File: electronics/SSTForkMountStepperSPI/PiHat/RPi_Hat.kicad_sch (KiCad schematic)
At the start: 32 parts, among them CON1 BARREL_JACK, J1 RJ12, J3 RA_STEP, J4 DEC_ENC, J5 RA_ENC, J6 DEC_STEP, Q1 Si2369DS, SW1 SW_SPST, U2 pololu_D24V22F5, U3 Teensy_4.0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

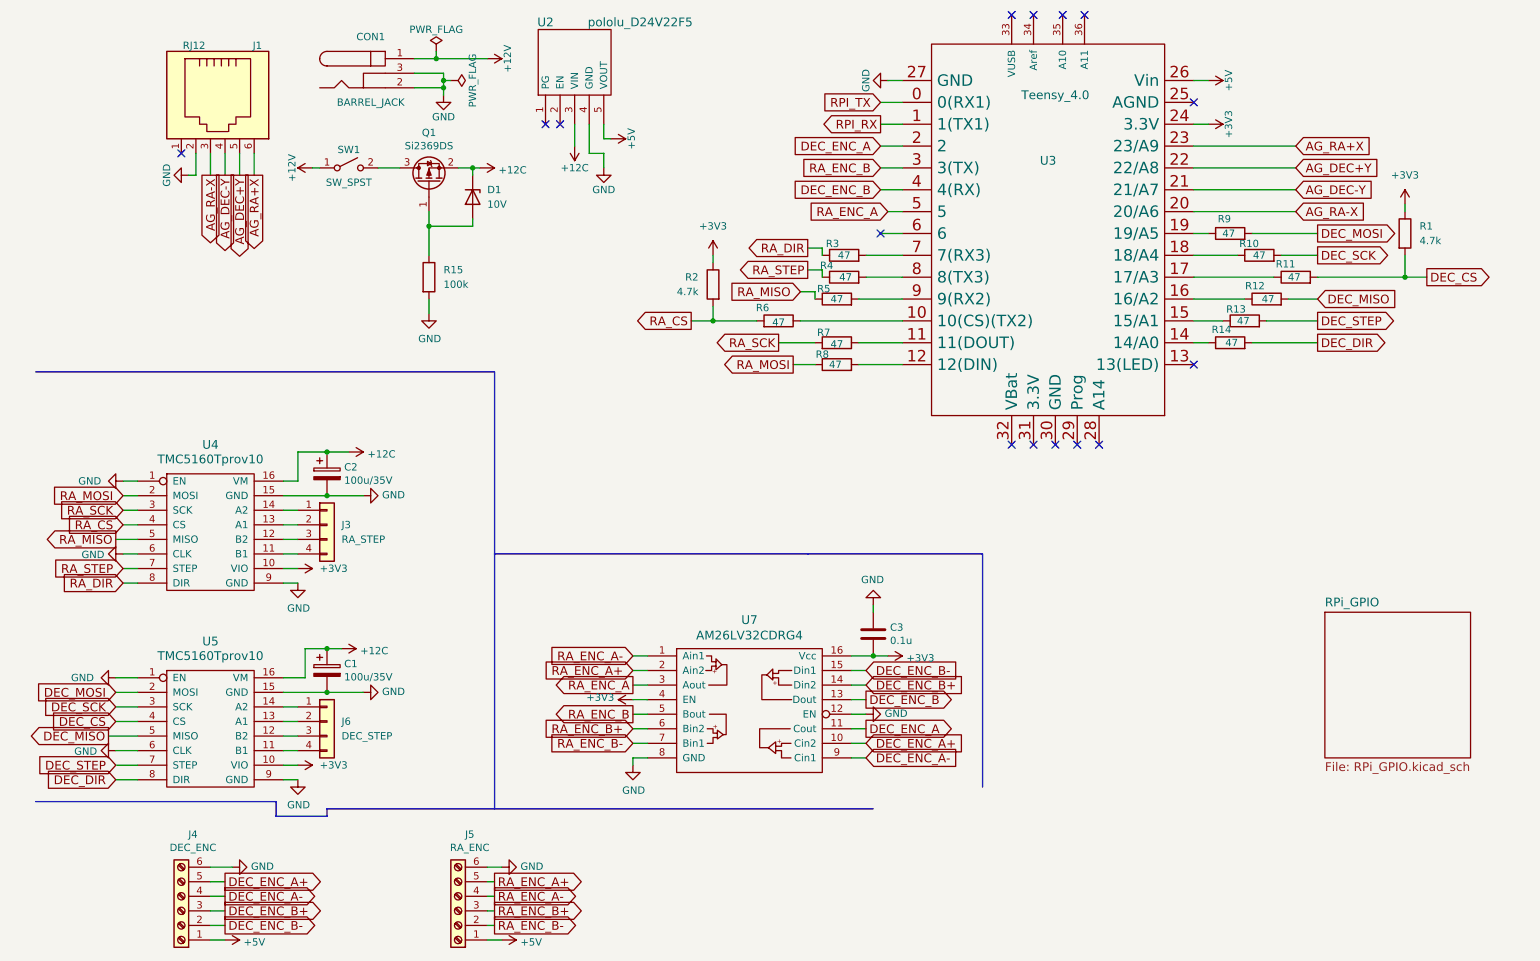
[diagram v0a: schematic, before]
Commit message: Fixed long commands to micro.
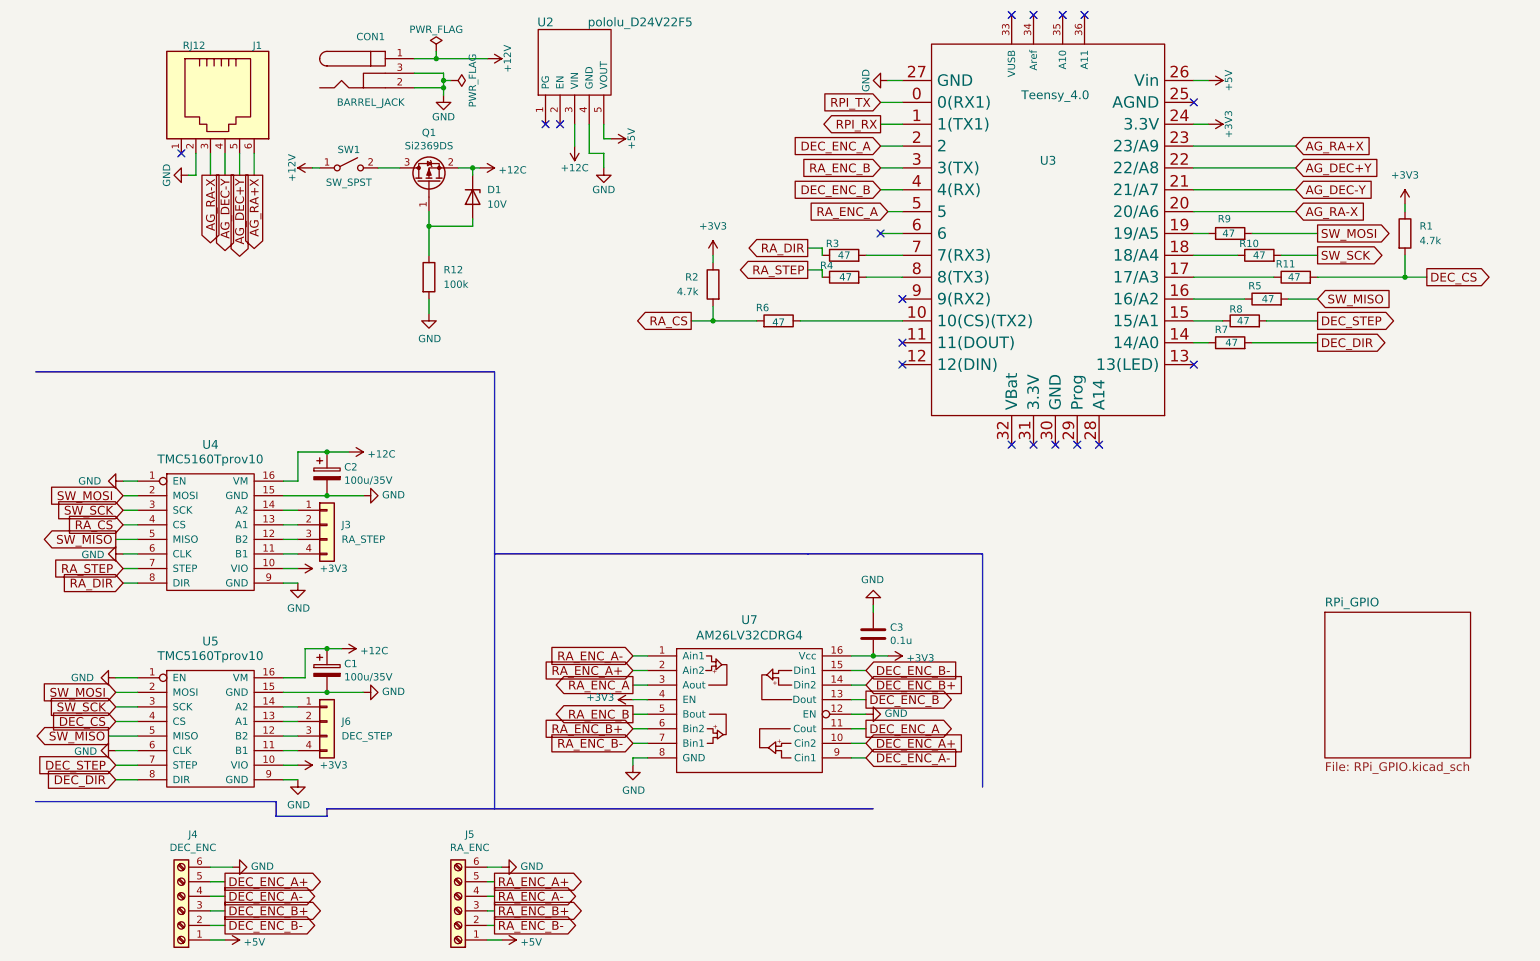
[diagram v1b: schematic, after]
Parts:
- removed R5, R7, R8: 47, Resistor_SMD:R_0603_1608Metric, symbol Device:R
- renumbered R15 to R12, R12 to R5, R14 to R7, R13 to R8
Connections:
- net RA_MISO is gone; now on net SW_MISO: U4.5 (MISO)
- net RA_MOSI is gone; now on net SW_MOSI: U4.2 (MOSI)
- net RA_SCK is gone; now on net SW_SCK: U4.3 (SCK)
- net DEC_MISO renamed SW_MISO
- net DEC_MOSI renamed SW_MOSI
- net DEC_SCK renamed SW_SCK
- no-connect marks 15 -> 18
